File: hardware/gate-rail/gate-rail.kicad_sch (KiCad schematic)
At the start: 20 parts, among them J1 RAIL-IDC, Q1 PT204-6B, Q2 PT204-6B, Q3 PT204-6B, Q4 PT204-6B, Q5 PT204-6B, Q6 PT204-6B

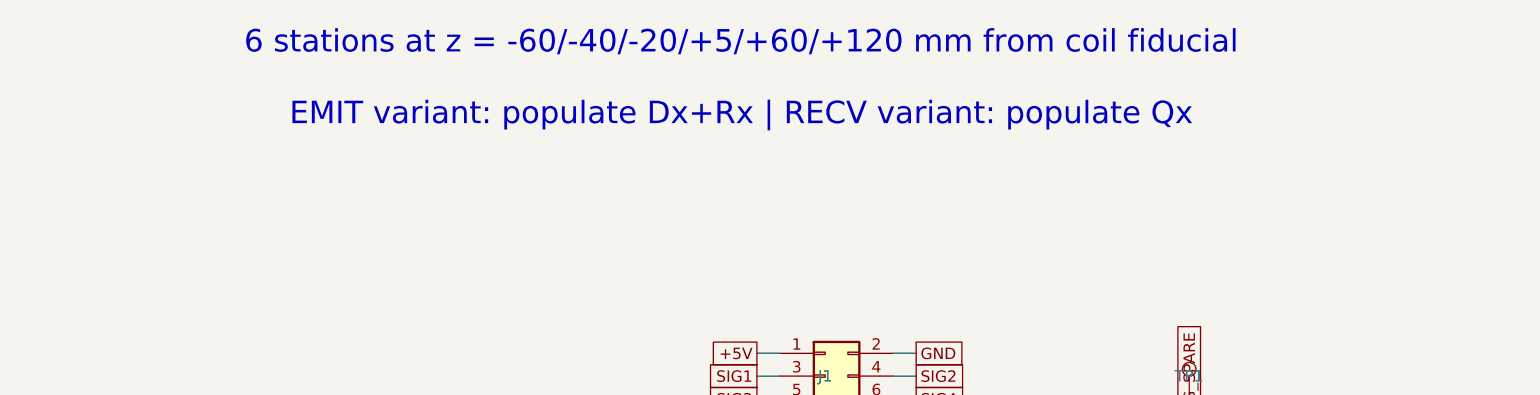
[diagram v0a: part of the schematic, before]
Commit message: Address external design review: boost FB + OVP redesign, BOM freeze
Review findings accepted and fixed (each verified by machine check):

1. Boost feedback network was wrong (confirmed: as-drawn spanned
   54-68V with PWM inverted vs the comment). Redesigned: RT/RB/RJ =
   100k/10k/9.1k with the exact transfer function documented in the
   schematic and design-calcs.md. PWM=0 (MCU-dead state) commands
   55.0V; full PWM commands 18.7V (below the 24.5V converter floor).
   New calcs.py asserts both endpoints.
2. OVP tripped at 55.6V, not the claimed 63V (confirmed). Redesigned:
   CJ431 (+/-0.5%) + 100k/4.3k 1% -> 60.5V nominal, 59.1-62.0V across
   tolerances. Protection ladder asserted in calcs.py: 55V operating
   < 59.1V trip-min, 62.0V trip-max < 63V cap rating - 1V. Operating
   ceiling deliberately reduced 60->55V to keep the bands disjoint.
3. BOM/schematic controller split-brain: bom.csv was stale
   (pre-UC3843 swap); regenerated from parts.py. Both now UC3843B.
4. High-power placeholders now real orderable parts (LCSC-verified):
   47R/5W SQM cement C5807995, dump redesigned to 2x 100R/10W cement
   in series C216413 (no 20-25W part stocked on LCSC; 5.3s to <5V),
   50mR/3W 2512 C2994645, 63V/35V electrolytics C28241/C176666, 10uH
   Sunlord C79272, MINI fuses+Keystone 3568 holders, buzzer, Pico
   sockets/breakout headers. Single documented exception: the 6.8k/2W
   bleed (CRH2512J6K80E04Z) is marked ORDER-REVIEW because LCSC's
   search is uncrawlable - validate.py allowlists it visibly.
5. validate.py pulled forward from the fab phase: fails on unknown
   footprints, blank LCSC on machine-placed parts, missing Variant
   fields, and duplicate refs; generates per-variant gate-rail BOMs
   (bom_rail_emit/recv.csv). Caught two bad footprint names.
6. Paralleling constraints now on the schematic (same-lot FETs,
   symmetric copper, <25mm gate loops, driver return at shunt star).
7. Fail-safe defaults hardened: MCU_FIRE and FIRE_GATED get explicit
   pulldow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
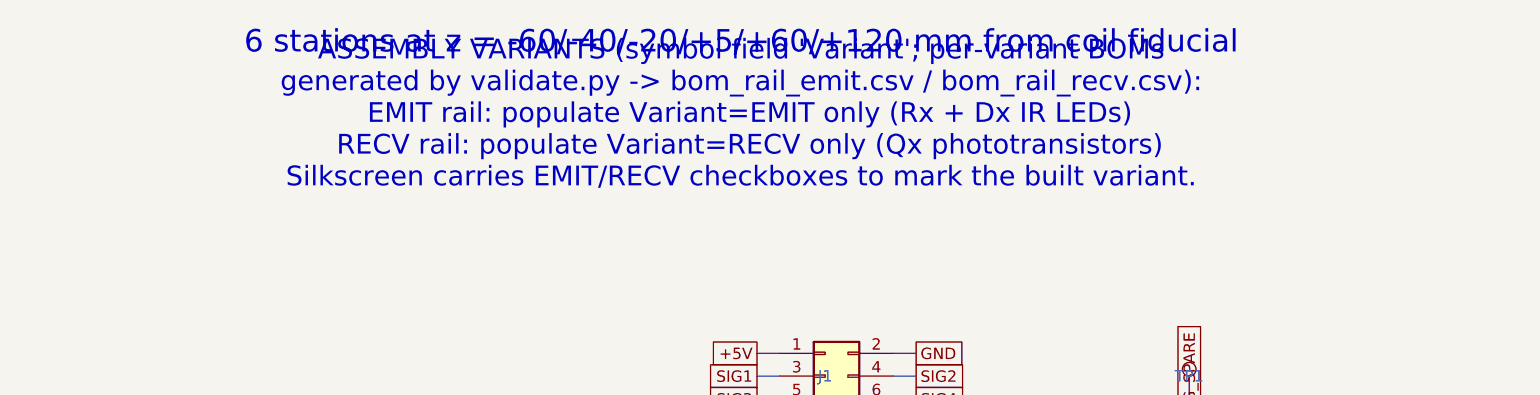
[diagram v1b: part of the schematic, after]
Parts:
- D1, D2, D3, D4, D5, D6: Variant (none) -> EMIT
- Q1, Q2, Q3, Q4, Q5, Q6: Variant (none) -> RECV
- R1, R2, R3, R4, R5, R6: LCSC (none) -> C22843; Variant (none) -> EMIT
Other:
- note added: "ASSEMBLY VARIANTS (symbol field 'Variant'; per-variant BOMs generated by validate.py -> bom_rail_emit.csv / bom_rail_recv.csv): EMIT rail: populate Variant=EMIT only (Rx + Dx IR LEDs) RECV rail: populate Variant=RECV only (Qx phototransistors) Silkscreen carries EMIT/RECV checkboxes to mark the built variant."
- note removed: "EMIT variant: populate Dx+Rx | RECV variant: populate Qx"

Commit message: Re-audit hygiene fixes: stale labels, COMMON variant, production gate
All six re-audit findings addressed:
1. Rail variant BOMs now include Variant=COMMON parts (J1 RAIL-IDC
   appears in both bom_rail_emit.csv and bom_rail_recv.csv).
2. design-calcs.md headings derive from V_BANK_MAX instead of
   hardcoded "60V" strings.
3. OVP reference wording unified to CJ431 +/-0.5% everywhere (the
   math already used ref_tol=0.005; text now matches).
4. Stale "57.2V OVP floor" magic number in the boost comment replaced
   with a reference to the calcs.py protection-ladder asserts.
5. validate.py --production mode: ORDER-REVIEW placeholder LCSC
   values fail (exit 1) at fab/assembly export; review mode warns.
   Verified: production exit code 1 on the 6.8k bleed placeholder.
6. Boost capability wording is now "24.5-55V operating (63V-rated
   bank)" in the schematic, sheet comments, and parts.py.

Re-verified: calcs 18/18 PASS, ERC 0 both projects, netlist
assertions pass, validate review-mode PASS with visible WARN,
rail BOMs 13/7 parts. PDFs refreshed.

Co-Authored-By: Claude Fable 5 <noreply@anthropic.com>
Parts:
- J1: Variant (none) -> COMMON
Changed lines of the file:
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@@
 			)
 		)
+		(property "Variant" "COMMON"
+			(at 39.37 59.69 0)
+			(show_name no)
+			(do_not_autoplace no)
+			(hide yes)
+			(effects
+				(font
+					(size 1.27 1.27)
+				)
+			)
+		)
 		(pin "1"
 		)
@@
 		(instances
 			(project "gate-rail"
-				(path "/a34b92c5-c2a8-4c39-919c-f149d21e3117"
+				(path "/a9b9b12f-3027-4477-a5f2-bbcba709feee"
 					(reference "J1")
 					(unit 1)
@@
 		(instances
 			(project "gate-rail"
-				(path "/a34b92c5-c2a8-4c39-919c-f149d21e3117"
+				(path "/a9b9b12f-3027-4477-a5f2-bbcba709feee"
 					(reference "TP1")
 					(unit 1)
@@
 		(instances
 			(project "gate-rail"
-				(path "/a34b92c5-c2a8-4c39-919c-f149d21e3117"
+				(path "/a9b9b12f-3027-4477-a5f2-bbcba709feee"
 					(reference "R1")
 					(unit 1)
@@
 		(instances
 			(project "gate-rail"
-				(path "/a34b92c5-c2a8-4c39-919c-f149d21e3117"
+				(path "/a9b9b12f-3027-4477-a5f2-bbcba709feee"
 					(reference "D1")
 					(unit 1)
@@
 		(instances
 			(project "gate-rail"
-				(path "/a34b92c5-c2a8-4c39-919c-f149d21e3117"
+				(path "/a9b9b12f-3027-4477-a5f2-bbcba709feee"
 					(reference "Q1")
 					(unit 1)
@@
 		(instances
 			(project "gate-rail"
-				(path "/a34b92c5-c2a8-4c39-919c-f149d21e3117"
+				(path "/a9b9b12f-3027-4477-a5f2-bbcba709feee"
 					(reference "R2")
 					(unit 1)
@@
 		(instances
 			(project "gate-rail"
-				(path "/a34b92c5-c2a8-4c39-919c-f149d21e3117"
+				(path "/a9b9b12f-3027-4477-a5f2-bbcba709feee"
 					(reference "D2")
 					(unit 1)
@@
 		(instances
 			(project "gate-rail"
-				(path "/a34b92c5-c2a8-4c39-919c-f149d21e3117"
+				(path "/a9b9b12f-3027-4477-a5f2-bbcba709feee"
 					(reference "Q2")
 					(unit 1)
@@
 		(instances
 			(project "gate-rail"
-				(path "/a34b92c5-c2a8-4c39-919c-f149d21e3117"
+				(path "/a9b9b12f-3027-4477-a5f2-bbcba709feee"
 					(reference "R3")
 					(unit 1)
@@
 		(instances
 			(project "gate-rail"
-				(path "/a34b92c5-c2a8-4c39-919c-f149d21e3117"
+				(path "/a9b9b12f-3027-4477-a5f2-bbcba709feee"
 					(reference "D3")
 					(unit 1)
@@
 		(instances
 			(project "gate-rail"
-				(path "/a34b92c5-c2a8-4c39-919c-f149d21e3117"
+				(path "/a9b9b12f-3027-4477-a5f2-bbcba709feee"
 					(reference "Q3")
 					(unit 1)
@@
 		(instances
 			(project "gate-rail"
-				(path "/a34b92c5-c2a8-4c39-919c-f149d21e3117"
+				(path "/a9b9b12f-3027-4477-a5f2-bbcba709feee"
 					(reference "R4")
 					(unit 1)
@@
 		(instances
 			(project "gate-rail"
-				(path "/a34b92c5-c2a8-4c39-919c-f149d21e3117"
+				(path "/a9b9b12f-3027-4477-a5f2-bbcba709feee"
 					(reference "D4")
 					(unit 1)
@@
 		(instances
 			(project "gate-rail"
-				(path "/a34b92c5-c2a8-4c39-919c-f149d21e3117"
+				(path "/a9b9b12f-3027-4477-a5f2-bbcba709feee"
 					(reference "Q4")
 					(unit 1)
@@
 		(instances
 			(project "gate-rail"
-				(path "/a34b92c5-c2a8-4c39-919c-f149d21e3117"
+				(path "/a9b9b12f-3027-4477-a5f2-bbcba709feee"
 					(reference "R5")
 					(unit 1)
@@
 		(instances
 			(project "gate-rail"
-				(path "/a34b92c5-c2a8-4c39-919c-f149d21e3117"
+				(path "/a9b9b12f-3027-4477-a5f2-bbcba709feee"
 					(reference "D5")
 					(unit 1)
@@
 		(instances
 			(project "gate-rail"
-				(path "/a34b92c5-c2a8-4c39-919c-f149d21e3117"
+				(path "/a9b9b12f-3027-4477-a5f2-bbcba709feee"
 					(reference "Q5")
 					(unit 1)
@@
 		(instances
 			(project "gate-rail"
-				(path "/a34b92c5-c2a8-4c39-919c-f149d21e3117"
+				(path "/a9b9b12f-3027-4477-a5f2-bbcba709feee"
 					(reference "R6")
 					(unit 1)
@@
 		(instances
 			(project "gate-rail"
-				(path "/a34b92c5-c2a8-4c39-919c-f149d21e3117"
+				(path "/a9b9b12f-3027-4477-a5f2-bbcba709feee"
 					(reference "D6")
 					(unit 1)
@@
 		(instances
 			(project "gate-rail"
-				(path "/a34b92c5-c2a8-4c39-919c-f149d21e3117"
+				(path "/a9b9b12f-3027-4477-a5f2-bbcba709feee"
 					(reference "Q6")
 					(unit 1)
@@
 		(instances
 			(project "gate-rail"
-				(path "/a34b92c5-c2a8-4c39-919c-f149d21e3117"
+				(path "/a9b9b12f-3027-4477-a5f2-bbcba709feee"
 					(reference "#FLG0001")
 					(unit 1)
@@
 		(instances
 			(project "gate-rail"
-				(path "/a34b92c5-c2a8-4c39-919c-f149d21e3117"
+				(path "/a9b9b12f-3027-4477-a5f2-bbcba709feee"
 					(reference "#FLG0002")
 					(unit 1)
@@
 		(instances
 			(project "gate-rail"
-				(path "/a34b92c5-c2a8-4c39-919c-f149d21e3117"
+				(path "/a9b9b12f-3027-4477-a5f2-bbcba709feee"
 					(reference "#PWR0003")
 					(unit 1)

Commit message: Gate-rail: fix 62 schematic-parity issues (metadata sync)
The rail board carried raw library footprint identities: gen_rail_pcb.py's
placement loop set only ref + pad nets, never FPID / Value / LCSC / Variant. So
every D/Q/R showed value "LED_D5.0mm" instead of "IR333C-A", bare footprint names
missing the library nickname, and no LCSC/Variant fields -> 41 mismatch + 19 field
+ 2 extra_footprint (H1/H2).

Fixes (mirroring the driver's gen_pcb.py place_all):
- load_netlist() now also reads <value> + LCSC + Variant fields into a meta map.
- Placement loop sets SetFPID(LIB_ID) + SetValue + SetField("LCSC"/"Variant"),
  keeping LCSC/Variant HIDDEN (SetField defaults to visible on silk -> was adding
  ~69 silk overlaps; hidden restores the 20-warning baseline).
- H1/H2 mounting holes flagged SetBoardOnly + SetExcludedFromBOM (exempt from
  extra_footprint parity), matching the driver.
- TP1 symbol marked in_bom=False so its exclude-from-BOM matches the footprint.

Result: kicad-cli --schematic-parity 0 / 0 electrical / 0 unconnected; ERC 0;
validate.py --production PASS; station-spacing assertion PASS; variant BOMs
regenerated (EMIT 13, RECV 7). Fully deterministic, no autorouter.

Co-Authored-By: Claude Opus 4.8 <noreply@anthropic.com>
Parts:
- TP1: now left out of the parts list
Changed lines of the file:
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@@
 		(instances
 			(project "gate-rail"
-				(path "/a9b9b12f-3027-4477-a5f2-bbcba709feee"
+				(path "/548dcc44-00dc-416f-8720-8f80dd51b293"
 					(reference "J1")
 					(unit 1)
@@
 		(unit 1)
 		(exclude_from_sim no)
-		(in_bom yes)
+		(in_bom no)
 		(on_board yes)
 		(dnp no)
@@
 		(instances
 			(project "gate-rail"
-				(path "/a9b9b12f-3027-4477-a5f2-bbcba709feee"
+				(path "/548dcc44-00dc-416f-8720-8f80dd51b293"
 					(reference "TP1")
 					(unit 1)
@@
 		(instances
 			(project "gate-rail"
-				(path "/a9b9b12f-3027-4477-a5f2-bbcba709feee"
+				(path "/548dcc44-00dc-416f-8720-8f80dd51b293"
 					(reference "R1")
 					(unit 1)
@@
 		(instances
 			(project "gate-rail"
-				(path "/a9b9b12f-3027-4477-a5f2-bbcba709feee"
+				(path "/548dcc44-00dc-416f-8720-8f80dd51b293"
 					(reference "D1")
 					(unit 1)
@@
 		(instances
 			(project "gate-rail"
-				(path "/a9b9b12f-3027-4477-a5f2-bbcba709feee"
+				(path "/548dcc44-00dc-416f-8720-8f80dd51b293"
 					(reference "Q1")
 					(unit 1)
@@
 		(instances
 			(project "gate-rail"
-				(path "/a9b9b12f-3027-4477-a5f2-bbcba709feee"
+				(path "/548dcc44-00dc-416f-8720-8f80dd51b293"
 					(reference "R2")
 					(unit 1)
@@
 		(instances
 			(project "gate-rail"
-				(path "/a9b9b12f-3027-4477-a5f2-bbcba709feee"
+				(path "/548dcc44-00dc-416f-8720-8f80dd51b293"
 					(reference "D2")
 					(unit 1)
@@
 		(instances
 			(project "gate-rail"
-				(path "/a9b9b12f-3027-4477-a5f2-bbcba709feee"
+				(path "/548dcc44-00dc-416f-8720-8f80dd51b293"
 					(reference "Q2")
 					(unit 1)
@@
 		(instances
 			(project "gate-rail"
-				(path "/a9b9b12f-3027-4477-a5f2-bbcba709feee"
+				(path "/548dcc44-00dc-416f-8720-8f80dd51b293"
 					(reference "R3")
 					(unit 1)
@@
 		(instances
 			(project "gate-rail"
-				(path "/a9b9b12f-3027-4477-a5f2-bbcba709feee"
+				(path "/548dcc44-00dc-416f-8720-8f80dd51b293"
 					(reference "D3")
 					(unit 1)
@@
 		(instances
 			(project "gate-rail"
-				(path "/a9b9b12f-3027-4477-a5f2-bbcba709feee"
+				(path "/548dcc44-00dc-416f-8720-8f80dd51b293"
 					(reference "Q3")
 					(unit 1)
@@
 		(instances
 			(project "gate-rail"
-				(path "/a9b9b12f-3027-4477-a5f2-bbcba709feee"
+				(path "/548dcc44-00dc-416f-8720-8f80dd51b293"
 					(reference "R4")
 					(unit 1)
@@
 		(instances
 			(project "gate-rail"
-				(path "/a9b9b12f-3027-4477-a5f2-bbcba709feee"
+				(path "/548dcc44-00dc-416f-8720-8f80dd51b293"
 					(reference "D4")
 					(unit 1)
@@
 		(instances
 			(project "gate-rail"
-				(path "/a9b9b12f-3027-4477-a5f2-bbcba709feee"
+				(path "/548dcc44-00dc-416f-8720-8f80dd51b293"
 					(reference "Q4")
 					(unit 1)
@@
 		(instances
 			(project "gate-rail"
-				(path "/a9b9b12f-3027-4477-a5f2-bbcba709feee"
+				(path "/548dcc44-00dc-416f-8720-8f80dd51b293"
 					(reference "R5")
 					(unit 1)
@@
 		(instances
 			(project "gate-rail"
-				(path "/a9b9b12f-3027-4477-a5f2-bbcba709feee"
+				(path "/548dcc44-00dc-416f-8720-8f80dd51b293"
 					(reference "D5")
 					(unit 1)
@@
 		(instances
 			(project "gate-rail"
-				(path "/a9b9b12f-3027-4477-a5f2-bbcba709feee"
+				(path "/548dcc44-00dc-416f-8720-8f80dd51b293"
 					(reference "Q5")
 					(unit 1)
@@
 		(instances
 			(project "gate-rail"
-				(path "/a9b9b12f-3027-4477-a5f2-bbcba709feee"
+				(path "/548dcc44-00dc-416f-8720-8f80dd51b293"
 					(reference "R6")
 					(unit 1)
@@
 		(instances
 			(project "gate-rail"
-				(path "/a9b9b12f-3027-4477-a5f2-bbcba709feee"
+				(path "/548dcc44-00dc-416f-8720-8f80dd51b293"
 					(reference "D6")
 					(unit 1)
@@
 		(instances
 			(project "gate-rail"
-				(path "/a9b9b12f-3027-4477-a5f2-bbcba709feee"
+				(path "/548dcc44-00dc-416f-8720-8f80dd51b293"
 					(reference "Q6")
 					(unit 1)
@@
 		(instances
 			(project "gate-rail"
-				(path "/a9b9b12f-3027-4477-a5f2-bbcba709feee"
+				(path "/548dcc44-00dc-416f-8720-8f80dd51b293"
 					(reference "#FLG0001")
 					(unit 1)
@@
 		(instances
 			(project "gate-rail"
-				(path "/a9b9b12f-3027-4477-a5f2-bbcba709feee"
+				(path "/548dcc44-00dc-416f-8720-8f80dd51b293"
 					(reference "#FLG0002")
 					(unit 1)
@@
 		(instances
 			(project "gate-rail"
-				(path "/a9b9b12f-3027-4477-a5f2-bbcba709feee"
+				(path "/548dcc44-00dc-416f-8720-8f80dd51b293"
 					(reference "#PWR0003")
 					(unit 1)

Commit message: Gate-rail review fixes: correct EMIT resistor part; opto-polarity gate + docs
Two independent reviews; reconciled:
- [P1, real] EMIT resistors were LCSC C22843 = 0603WAF1501T5E = 1.5k, not 150ohm
  (LEDs would run ~2.5mA, break-beam margin collapses). Root cause: gen_gate_rail
  hardcoded the wrong C-number. Fixed to C22808 (0603WAF1500T5E, 150ohm, JLC basic
  -- matches the driver's own 150->C22808 mapping).
- [P0, DISPUTED -> board is correct, do NOT swap] Reviewer 1 called the IR333C-A /
  PT204-6B reversed (Everlight pin1 = anode/emitter, opposite KiCad convention);
  reviewer 2 said correct via flat-to-flat insertion. Verified from the footprint:
  LED_D5.0mm pad1 is the rect pad with the polarity flat silk on the pad1 side, and
  the board wires pad1(flat/cathode)->GND, anode->LEDA (Q: pad1/flat/collector->SIG,
  emitter->GND). The board is correctly wired for flat-oriented placement; swapping
  the nets would REVERSE a correct board, so nets are unchanged. Added a mandatory
  "confirm opto polarity in the assembly preview" gate to ORDER_NOTES as the backstop.
- [P2/nits] Docs: J1 matches driver J7 pin-for-pin; J6 is power-only, never plug a
  RECV board into J6 (RAIL_OVERVIEW). Fixed "2 vias both +5V" -> "+5V and SIG_SPARE"
  and ~132mA -> ~144mA (24mA/LED).

Board re-run: DRC 0 parity / 0 electrical / 0 unconnected; validate --production
PASS; variant CPLs unchanged (EMIT 13, RECV 7).

Co-Authored-By: Claude Opus 4.8 <noreply@anthropic.com>
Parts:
- R1, R2, R3, R4, R5, R6: LCSC C22843 -> C22808
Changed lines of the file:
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@@
 		(instances
 			(project "gate-rail"
-				(path "/548dcc44-00dc-416f-8720-8f80dd51b293"
+				(path "/c7c35b54-88a7-43c7-983a-3175b4b22b62"
 					(reference "J1")
 					(unit 1)
@@
 		(instances
 			(project "gate-rail"
-				(path "/548dcc44-00dc-416f-8720-8f80dd51b293"
+				(path "/c7c35b54-88a7-43c7-983a-3175b4b22b62"
 					(reference "TP1")
 					(unit 1)
@@
 			)
 		)
-		(property "LCSC" "C22843"
+		(property "LCSC" "C22808"
 			(at 39.37 100.33 0)
 			(show_name no)
@@
 		(instances
 			(project "gate-rail"
-				(path "/548dcc44-00dc-416f-8720-8f80dd51b293"
+				(path "/c7c35b54-88a7-43c7-983a-3175b4b22b62"
 					(reference "R1")
 					(unit 1)
@@
 		(instances
 			(project "gate-rail"
-				(path "/548dcc44-00dc-416f-8720-8f80dd51b293"
+				(path "/c7c35b54-88a7-43c7-983a-3175b4b22b62"
 					(reference "D1")
 					(unit 1)
@@
 		(instances
 			(project "gate-rail"
-				(path "/548dcc44-00dc-416f-8720-8f80dd51b293"
+				(path "/c7c35b54-88a7-43c7-983a-3175b4b22b62"
 					(reference "Q1")
 					(unit 1)
@@
 			)
 		)
-		(property "LCSC" "C22843"
+		(property "LCSC" "C22808"
 			(at 74.93 100.33 0)
 			(show_name no)
@@
 		(instances
 			(project "gate-rail"
-				(path "/548dcc44-00dc-416f-8720-8f80dd51b293"
+				(path "/c7c35b54-88a7-43c7-983a-3175b4b22b62"
 					(reference "R2")
 					(unit 1)
@@
 		(instances
 			(project "gate-rail"
-				(path "/548dcc44-00dc-416f-8720-8f80dd51b293"
+				(path "/c7c35b54-88a7-43c7-983a-3175b4b22b62"
 					(reference "D2")
 					(unit 1)
@@
 		(instances
 			(project "gate-rail"
-				(path "/548dcc44-00dc-416f-8720-8f80dd51b293"
+				(path "/c7c35b54-88a7-43c7-983a-3175b4b22b62"
 					(reference "Q2")
 					(unit 1)
@@
 			)
 		)
-		(property "LCSC" "C22843"
+		(property "LCSC" "C22808"
 			(at 110.49 100.33 0)
 			(show_name no)
@@
 		(instances
 			(project "gate-rail"
-				(path "/548dcc44-00dc-416f-8720-8f80dd51b293"
+				(path "/c7c35b54-88a7-43c7-983a-3175b4b22b62"
 					(reference "R3")
 					(unit 1)
@@
 		(instances
 			(project "gate-rail"
-				(path "/548dcc44-00dc-416f-8720-8f80dd51b293"
+				(path "/c7c35b54-88a7-43c7-983a-3175b4b22b62"
 					(reference "D3")
 					(unit 1)
@@
 		(instances
 			(project "gate-rail"
-				(path "/548dcc44-00dc-416f-8720-8f80dd51b293"
+				(path "/c7c35b54-88a7-43c7-983a-3175b4b22b62"
 					(reference "Q3")
 					(unit 1)
@@
 			)
 		)
-		(property "LCSC" "C22843"
+		(property "LCSC" "C22808"
 			(at 144.78 100.33 0)
 			(show_name no)
@@
 		(instances
 			(project "gate-rail"
-				(path "/548dcc44-00dc-416f-8720-8f80dd51b293"
+				(path "/c7c35b54-88a7-43c7-983a-3175b4b22b62"
 					(reference "R4")
 					(unit 1)
@@
 		(instances
 			(project "gate-rail"
-				(path "/548dcc44-00dc-416f-8720-8f80dd51b293"
+				(path "/c7c35b54-88a7-43c7-983a-3175b4b22b62"
 					(reference "D4")
 					(unit 1)
@@
 		(instances
 			(project "gate-rail"
-				(path "/548dcc44-00dc-416f-8720-8f80dd51b293"
+				(path "/c7c35b54-88a7-43c7-983a-3175b4b22b62"
 					(reference "Q4")
 					(unit 1)
@@
 			)
 		)
-		(property "LCSC" "C22843"
+		(property "LCSC" "C22808"
 			(at 180.34 100.33 0)
 			(show_name no)
@@
 		(instances
 			(project "gate-rail"
-				(path "/548dcc44-00dc-416f-8720-8f80dd51b293"
+				(path "/c7c35b54-88a7-43c7-983a-3175b4b22b62"
 					(reference "R5")
 					(unit 1)
@@
 		(instances
 			(project "gate-rail"
-				(path "/548dcc44-00dc-416f-8720-8f80dd51b293"
+				(path "/c7c35b54-88a7-43c7-983a-3175b4b22b62"
 					(reference "D5")
 					(unit 1)
@@
 		(instances
 			(project "gate-rail"
-				(path "/548dcc44-00dc-416f-8720-8f80dd51b293"
+				(path "/c7c35b54-88a7-43c7-983a-3175b4b22b62"
 					(reference "Q5")
 					(unit 1)
@@
 			)
 		)
-		(property "LCSC" "C22843"
+		(property "LCSC" "C22808"
 			(at 214.63 100.33 0)
 			(show_name no)
@@
 		(instances
 			(project "gate-rail"
-				(path "/548dcc44-00dc-416f-8720-8f80dd51b293"
+				(path "/c7c35b54-88a7-43c7-983a-3175b4b22b62"
 					(reference "R6")
 					(unit 1)
@@
 		(instances
 			(project "gate-rail"
-				(path "/548dcc44-00dc-416f-8720-8f80dd51b293"
+				(path "/c7c35b54-88a7-43c7-983a-3175b4b22b62"
 					(reference "D6")
 					(unit 1)
@@
 		(instances
 			(project "gate-rail"
-				(path "/548dcc44-00dc-416f-8720-8f80dd51b293"
+				(path "/c7c35b54-88a7-43c7-983a-3175b4b22b62"
 					(reference "Q6")
 					(unit 1)
@@
 		(instances
 			(project "gate-rail"
-				(path "/548dcc44-00dc-416f-8720-8f80dd51b293"
+				(path "/c7c35b54-88a7-43c7-983a-3175b4b22b62"
 					(reference "#FLG0001")
 					(unit 1)
@@
 		(instances
 			(project "gate-rail"
-				(path "/548dcc44-00dc-416f-8720-8f80dd51b293"
+				(path "/c7c35b54-88a7-43c7-983a-3175b4b22b62"
 					(reference "#FLG0002")
 					(unit 1)
@@
 		(instances
 			(project "gate-rail"
-				(path "/548dcc44-00dc-416f-8720-8f80dd51b293"
+				(path "/c7c35b54-88a7-43c7-983a-3175b4b22b62"
 					(reference "#PWR0003")
 					(unit 1)
